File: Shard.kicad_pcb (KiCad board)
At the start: 4 copper layers, 54.6 x 46.3 mm, 52 parts, among them J1 USB_C_Receptacle_USB2.0_16P, J2 Conn_01x08, J3 Conn_01x08, J4 Conn_01x08, J5 Conn_01x08, SW1 SW_Push, SW2 SW_Push, U1 ESP32-S3, U2 USBLC6-2P6, U3 TLV76733DRVx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

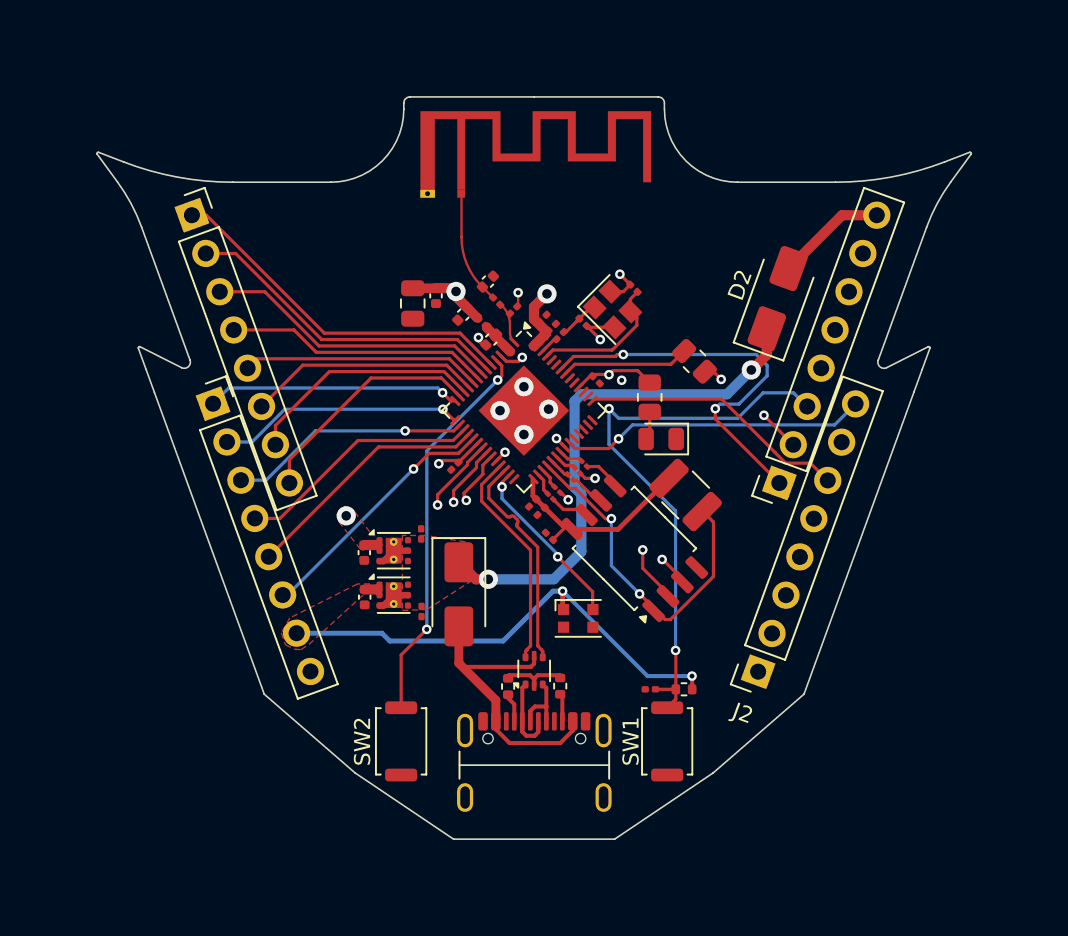
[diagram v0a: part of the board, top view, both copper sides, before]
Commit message: Add stitching vias, checked DRC rules
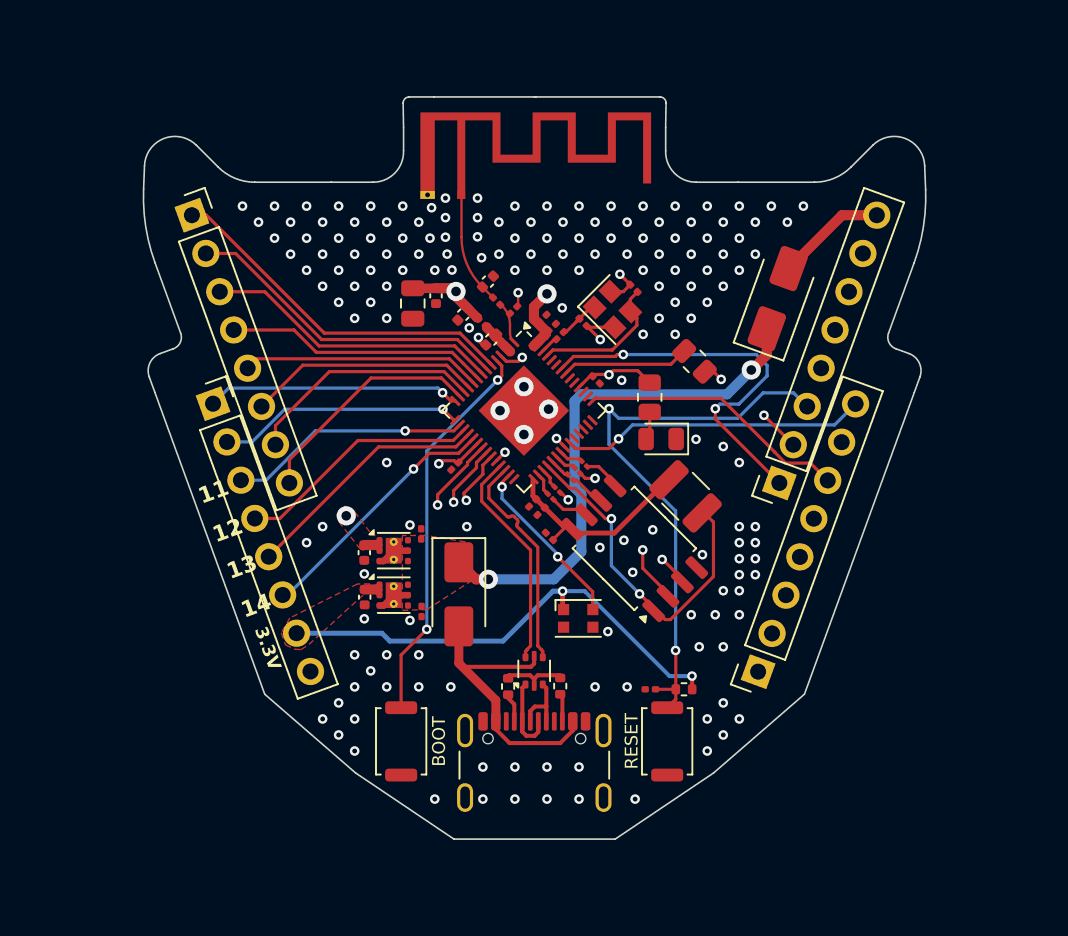
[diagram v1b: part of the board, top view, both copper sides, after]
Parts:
- moved R5 0.08 mm to (156.7, 99.1)
- moved ANT1 0.08 mm to (142.7, 80.3)
- renumbered SW2 to BOOT, SW1 to RESET
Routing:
- net +3.3V: track 56.6 -> 55.9 mm
- net GND: vias 9 -> 171
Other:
- board size 54.6 x 46.3 mm -> 48.8 x 46.3 mm
- board text added: "10"
- board text added: "11"
- board text added: "12"
- board text added: "13"
- board text added: "14"
- board text added: "3.3V"
- board text added: "9"
- board text added: "R12"

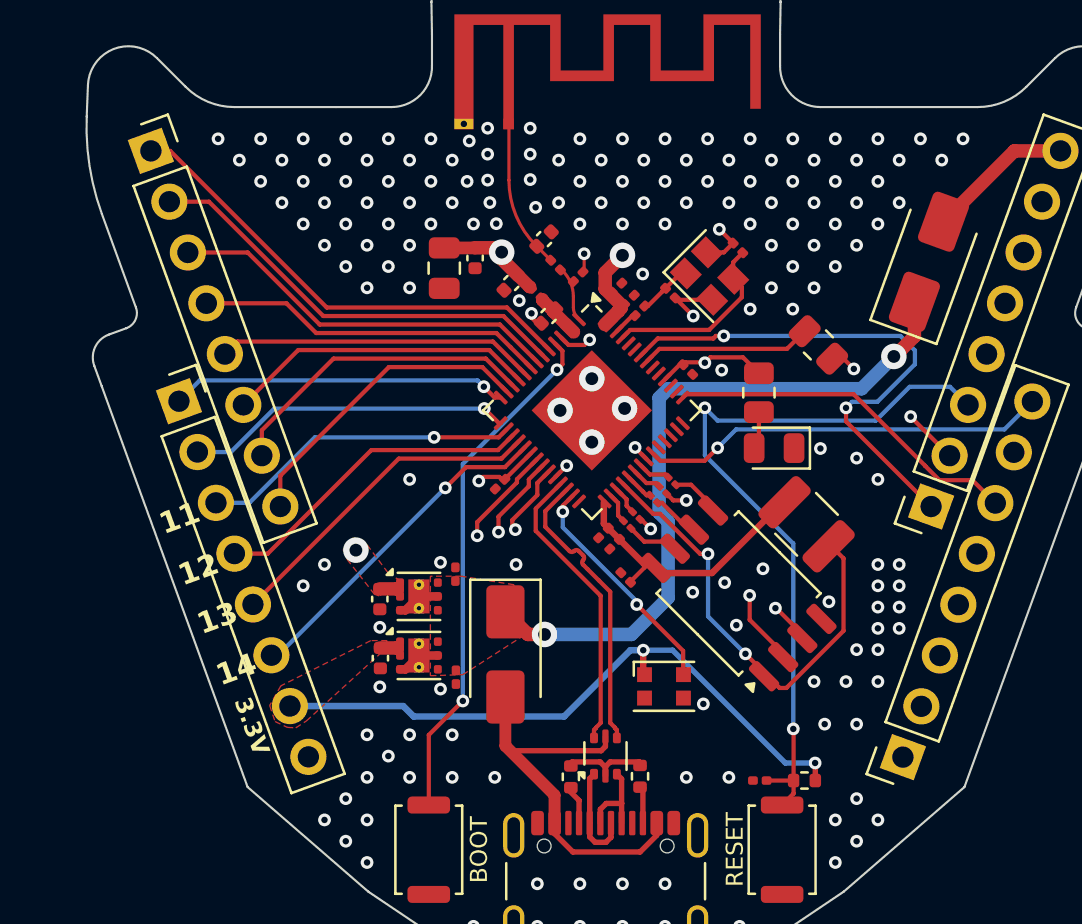
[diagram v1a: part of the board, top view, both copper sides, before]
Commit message: Add pinout to bottom silkscreen
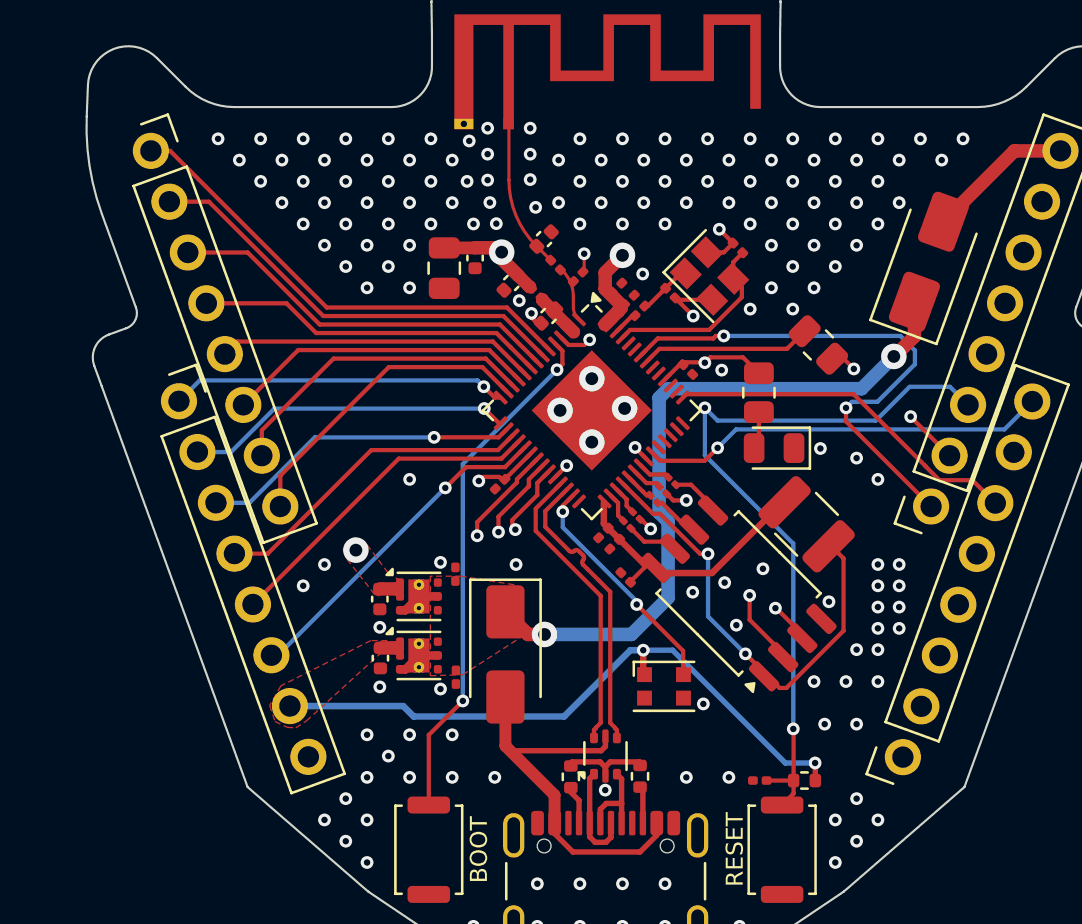
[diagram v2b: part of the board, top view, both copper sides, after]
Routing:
- net GND: vias 171 -> 172
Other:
- board text added: "1"
- board text added: "15"
- board text added: "16"
- board text added: "17"
- board text added: "18"
- board text added: "2"
- board text added: "3"
- board text added: "38"
- board text added: "4"
- board text added: "47"
- board text added: "48"
- board text added: "5"
- board text added: "6"
- board text added: "7"
- board text added: "8"
- board text added: "GND"
- board text added: "RESET"
- board text added: "RX"
- board text added: "TX"
- board text added: "VIN"

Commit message: Add production files
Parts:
- added G***: LOGO, LOGO, F.Cu at (134.3, 92.5)
- added REF**: OSHW-Logo2_7.3x6mm_SilkScreen, Symbol:OSHW-Logo2_7.3x6mm_SilkScreen, B.Cu at (147.2, 110.7)
- moved D3 0.10 mm to (155.1, 95.6)
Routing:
- net /7: track 14.9 -> 14.2 mm
- net GND: vias 172 -> 154
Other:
- board text added: "Designed with love by Ettore M. 07/24 REV 1"

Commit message: Fixed some things
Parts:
- R10, R6, R7, R8, R9: footprint Resistor_SMD:R_01005_0402Metric -> Resistor_SMD:R_0201_0603Metric
- moved R8 0.30 mm to (150.5, 96.8)
- moved C10 0.20 mm to (147.5, 100.2)
- moved C9 0.20 mm to (147.0, 99.7)
- moved R9 0.15 mm to (148.7, 98.5)
- moved R7 0.12 mm to (150.0, 97.4)
- moved R10 0.12 mm to (148.1, 99.2)
- moved R6 0.06 mm to (149.4, 97.9)
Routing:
- net GND: track 15.8 -> 15.3 mm

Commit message: Fix design errors & update README
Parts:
- turned D4 to 180 degrees
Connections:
- D4 pad 1: /E3.3V -> unconnected-(D4-DO-Pad1)
- D4 pad 2: unconnected-(D4-DOUT-Pad2) -> GND
- D4 pad 3: GND -> /21
- D4 pad 4: /21 -> VBUS
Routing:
- net VBUS: track 20.2 -> 24.6 mm
- net /E3.3V: track 83.3 -> 79.5 mm, vias 2 -> 1
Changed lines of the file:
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@@
 	(net 13 "Net-(D2-A)")
 	(net 14 "Net-(D3-A)")
-	(net 15 "unconnected-(D4-DOUT-Pad2)")
+	(net 15 "unconnected-(D4-DO-Pad1)")
 	(net 16 "/21")
 	(net 17 "/D_N")
@@
 	(net 74 "unconnected-(U1-MTDO-Pad45)")
 	(net 75 "unconnected-(J1-SHIELD-PadS1)")
-	(net 76 "unconnected-(J1-SHIELD-PadS1)_0")
+	(net 76 "unconnected-(J1-SHIELD-PadS1)_3")
 	(net 77 "unconnected-(J1-SHIELD-PadS1)_2")
 	(footprint "Diode_SMD:D_SMA"
@@
 	(footprint "LED_SMD:LED_WS2812B-2020_PLCC4_2.0x2.0mm"
 		(layer "F.Cu")
-		(at 149.95 106.725)
+		(at 149.95 106.725 180)
 		(descr "2.0mm x 2.0mm Addressable RGB LED NeoPixel Nano, 12 mA, https://cdn-shop.adafruit.com/product-files/4684/4684_WS2812B-2020_V1.3_EN.pdf")
 		(tags "LED RGB NeoPixel Nano PLCC-4 2020")
 		(property "Reference" "D4"
-			(at -0.2 -1.34 0)
+			(at -0.2 -1.34 360)
 			(layer "F.SilkS")
 			(hide yes)
@@
 		)
 		(property "Value" "WS2812B"
-			(at -2.75 2.625 0)
+			(at -2.75 2.625 360)
 			(layer "F.Fab")
 			(effects
@@
 		)
 		(property "Footprint" "LED_SMD:LED_WS2812B-2020_PLCC4_2.0x2.0mm"
-			(at 0 0 0)
+			(at 0 0 180)
 			(unlocked yes)
 			(layer "F.Fab")
@@
 		)
 		(property "Datasheet" "https://cdn-shop.adafruit.com/datasheets/WS2812B.pdf"
-			(at 0 0 0)
+			(at 0 0 180)
 			(unlocked yes)
 			(layer "F.Fab")
@@
 		)
 		(property "Description" "RGB LED with integrated controller"
-			(at 0 0 0)
+			(at 0 0 180)
 			(unlocked yes)
 			(layer "F.Fab")
@@
 		)
 		(property "REF" "C965555"
-			(at 0 0 0)
+			(at 0 0 180)
 			(unlocked yes)
 			(layer "F.Fab")
@@
 		(attr smd)
 		(fp_line
-			(start -1.42 -1.15)
-			(end -1.42 -0.5)
+			(start -1.42 1.15)
+			(end 1.42 1.15)
 			(stroke
 				(width 0.12)
@@
 		)
 		(fp_line
-			(start -1.42 1.15)
-			(end 1.42 1.15)
+			(start -1.42 -1.15)
+			(end -1.42 -0.5)
 			(stroke
 				(width 0.12)
@@
 		)
 		(fp_line
-			(start -1.52 -1.25)
-			(end -1.52 1.25)
+			(start 1.52 1.25)
+			(end 1.52 -1.25)
 			(stroke
 				(width 0.05)
@@
 		)
 		(fp_line
-			(start -1.52 1.25)
-			(end 1.52 1.25)
+			(start 1.52 -1.25)
+			(end -1.52 -1.25)
 			(stroke
 				(width 0.05)
@@
 		)
 		(fp_line
-			(start 1.52 -1.25)
-			(end -1.52 -1.25)
+			(start -1.52 1.25)
+			(end 1.52 1.25)
 			(stroke
 				(width 0.05)
@@
 		)
 		(fp_line
-			(start 1.52 1.25)
-			(end 1.52 -1.25)
+			(start -1.52 -1.25)
+			(end -1.52 1.25)
 			(stroke
 				(width 0.05)
@@
 		)
 		(fp_line
-			(start -1.1 -0.45)
-			(end -1.1 1)
+			(start 1.1 -1)
+			(end 1.1 1)
 			(stroke
 				(width 0.1)
@@
 		)
 		(fp_line
-			(start -1.1 1)
-			(end 1.1 1)
+			(start 1.1 -1)
+			(end -0.55 -1)
 			(stroke
 				(width 0.1)
@@
 		)
 		(fp_line
-			(start 1.1 -1)
-			(end -0.55 -1)
+			(start -1.1 1)
+			(end 1.1 1)
 			(stroke
 				(width 0.1)
@@
 		)
 		(fp_line
-			(start 1.1 -1)
-			(end 1.1 1)
+			(start -1.1 -0.45)
+			(end -1.1 1)
 			(stroke
 				(width 0.1)
@@
 		)
 		(fp_rect
-			(start -0.5 -1)
-			(end -0.05 -0.45)
+			(start -0.5 0.4)
+			(end -0.05 1)
 			(stroke
 				(width 0.1)
@@
 		)
 		(fp_rect
-			(start -0.5 0.4)
-			(end -0.05 1)
+			(start -0.5 -1)
+			(end -0.05 -0.45)
 			(stroke
 				(width 0.1)
@@
 		)
 		(fp_text user "${REFERENCE}"
-			(at 0 0 0)
+			(at 0 0 360)
 			(layer "F.Fab")
 			(effects
@@
 		)
 		(pad "1" smd rect
-			(at -0.915 -0.55)
+			(at -0.915 -0.55 180)
 			(size 0.7 0.7)
 			(layers "F.Cu" "F.Paste" "F.Mask")
-			(net 7 "/E3.3V")
-			(pinfunction "VDD")
-			(pintype "power_in")
+			(net 15 "unconnected-(D4-DO-Pad1)")
+			(pinfunction "DO")
+			(pintype "output+no_connect")
 		)
 		(pad "2" smd rect
-			(at -0.915 0.55)
+			(at -0.915 0.55 180)
 			(size 0.7 0.7)
 			(layers "F.Cu" "F.Paste" "F.Mask")
-			(net 15 "unconnected-(D4-DOUT-Pad2)")
-			(pinfunction "DOUT")
-			(pintype "output+no_connect")
+			(net 2 "GND")
+			(pinfunction "GND")
+			(pintype "power_out")
 		)
 		(pad "3" smd rect
-			(at 0.915 0.55)
+			(at 0.915 0.55 180)
 			(size 0.7 0.7)
 			(layers "F.Cu" "F.Paste" "F.Mask")
-			(net 2 "GND")
-			(pinfunction "VSS")
-			(pintype "power_in")
+			(net 16 "/21")
+			(pinfunction "DI")
+			(pintype "input")
 		)
 		(pad "4" smd rect
-			(at 0.915 -0.55)
+			(at 0.915 -0.55 180)
 			(size 0.7 0.7)
 			(layers "F.Cu" "F.Paste" "F.Mask")
-			(net 16 "/21")
-			(pinfunction "DIN")
-			(pintype "input")
-		)
-		(model "${KICAD8_3DMODEL_DIR}/LED_SMD.3dshapes/LED_WS2812B-2020_PLCC4_2.0x2.0mm.wrl"
-			(offset
-				(xyz 0 0 0)
-			)
-			(scale
-				(xyz 1 1 1)
-			)
-			(rotate
-				(xyz 0 0 0)
-			)
+			(net 12 "VBUS")
+			(pinfunction "VCC")
+			(pintype "power_in")
 		)
-		(model "${KICAD8_3DMODEL_DIR}/LED_SMD.3dshapes/LED_WS2812B_PLCC4_5.0x5.0mm_P3.2mm.step"
+		(model "${KICAD8_3DMODEL_DIR}/LED_SMD.3dshapes/LED_WS2812B-Mini_PLCC4_3.5x3.5mm.wrl"
 			(offset
 				(xyz 0 0 0)
 			)
 			(scale
-				(xyz 0.4 0.4 0.3)
+				(xyz 0.6 0.6 0.3)
 			)
 			(rotate
@@
 			(layers "*.Cu" "*.Mask" "F.Paste")
 			(remove_unused_layers no)
-			(net 77 "unconnected-(J1-SHIELD-PadS1)_2")
+			(net 76 "unconnected-(J1-SHIELD-PadS1)_3")
 			(pinfunction "SHIELD")
 			(pintype "passive+no_connect")
@@
 			(layers "*.Cu" "*.Mask" "F.Paste")
 			(remove_unused_layers no)
-			(net 21 "unconnected-(J1-SHIELD-PadS1)_1")
+			(net 77 "unconnected-(J1-SHIELD-PadS1)_2")
 			(pinfunction "SHIELD")
 			(pintype "passive+no_connect")
@@
 			(layers "*.Cu" "*.Mask" "F.Paste")
 			(remove_unused_layers no)
-			(net 76 "unconnected-(J1-SHIELD-PadS1)_0")
+			(net 21 "unconnected-(J1-SHIELD-PadS1)_1")
 			(pinfunction "SHIELD")
 			(pintype "passive+no_connect")
@@
 	)
 	(via
-		(at 151.6 108)
+		(at 151.8 106.2)
 		(size 0.6)
 		(drill 0.3)
@@
 	)
 	(segment
-		(start 148.975 106.115)
-		(end 149.035 106.175)
-		(width 0.3048)
-		(layer "F.Cu")
-		(net 7)
-	)
-	(segment
 		(start 137.415 104.92)
 		(end 137.42 104.925)
@@
 	)
 	(segment
-		(start 148.975 105.025)
-		(end 148.975 106.115)
-		(width 0.3048)
-		(layer "F.Cu")
-		(net 7)
-	)
-	(segment
 		(start 157.06 111.15)
 		(end 157.06 110.335)
@@
 		(net 7)
 	)
-	(via
-		(at 148.975 105.025)
-		(size 0.6)
-		(drill 0.3)
-		(layers "F.Cu" "B.Cu")
-		(net 7)
-	)
 	(segment
 		(start 132.856269 105.822369)
@@
 	)
 	(segment
-		(start 138.19 108.14)
-		(end 145.26 108.14)
-		(width 0.3048)
-		(layer "B.Cu")
-		(net 7)
-	)
-	(segment
-		(start 157.05 110.325)
-		(end 155.65 110.325)
-		(width 0.254)
-		(layer "B.Cu")
-		(net 7)
-	)
-	(segment
-		(start 150.35 105.025)
-		(end 148.975 105.025)
-		(width 0.254)
-		(layer "B.Cu")
-		(net 7)
-	)
-	(segment
-		(start 137.7 107.65)
-		(end 138.19 108.14)
+		(start 132.8 108.075)
+		(end 132.375 107.65)
 		(width 0.3048)
 		(layer "B.Cu")
@@
 	)
 	(segment
-		(start 145.26 108.14)
-		(end 148.375 105.025)
+		(start 150.8 108.075)
+		(end 132.8 108.075)
 		(width 0.3048)
 		(layer "B.Cu")
@@
 	)
 	(segment
-		(start 155.65 110.325)
-		(end 150.35 105.025)
+		(start 150.8 108.086712)
+		(end 153.038288 110.325)
 		(width 0.254)
 		(layer "B.Cu")
@@
 	)
 	(segment
-		(start 132.375 107.65)
-		(end 137.7 107.65)
-		(width 0.3048)
+		(start 153.038288 110.325)
+		(end 157.05 110.325)
+		(width 0.254)
 		(layer "B.Cu")
 		(net 7)
 	)
 	(segment
-		(start 148.375 105.025)
-		(end 148.975 105.025)
-		(width 0.3048)
+		(start 150.8 108.075)
+		(end 150.8 108.086712)
+		(width 0.254)
 		(layer "B.Cu")
 		(net 7)
@@
 	)
 	(segment
+		(start 149.035 108.700128)
+		(end 149.035 107.275)
+		(width 0.254)
+		(layer "F.Cu")
+		(net 12)
+	)
+	(segment
 		(start 147.2 109.55)
 		(end 147 109.75)
@@
 	)
 	(segment
+		(start 147.4 109.75)
+		(end 147.6 109.75)
+		(width 0.254)
+		(layer "F.Cu")
+		(net 12)
+	)
+	(segment
 		(start 142.5 109.525)
 		(end 142.5 107.225002)
@@
 	)
 	(segment
+		(start 147.985128 109.75)
+		(end 149.035 108.700128)
+		(width 0.254)
+		(layer "F.Cu")
+		(net 12)
+	)
+	(segment
+		(start 147.6 109.75)
+		(end 147.985128 109.75)
+		(width 0.254)
+		(layer "F.Cu")
+		(net 12)
+	)
+	(segment
 		(start 149.61 113.15)
 		(end 149.61 113.722222)
@@
 	)
 	(segment
+		(start 147 109.75)
+		(end 147.6 109.75)
+		(width 0.254)
+		(layer "F.Cu")
+		(net 12)
+	)
+	(segment
+		(start 147.2 109.55)
+		(end 147.4 109.75)
+		(width 0.254)
+		(layer "F.Cu")
+		(net 12)
+	)
+	(segment
 		(start 142.875001 107.225001)
 		(end 142.5 107.225001)
@@
 	)
 	(segment
-		(start 150.85 105.060001)
-		(end 150.85 105.9)
+		(start 148.975 106.115)
+		(end 149.035 106.175)
+		(width 0.3048)
+		(layer "F.Cu")
+		(net 16)
+	)
+	(segment
+		(start 148.669999 102.880001)
+		(end 148.67 102.880001)
 		(width 0.2)
 		(layer "F.Cu")
@@
 	)
 	(segment
-		(start 148.67 102.880001)
-		(end 150.85 105.060001)
+		(start 149.035 103.245001)
+		(end 149.035 106.175)
 		(width 0.2)
 		(layer "F.Cu")
@@
 	)
 	(segment
-		(start 148.669999 102.880001)
-		(end 148.67 102.880001)
+		(start 148.67 102.880001)
+		(end 149.035 103.245001)
 		(width 0.2)
 		(layer "F.Cu")
